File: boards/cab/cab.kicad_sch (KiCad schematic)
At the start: 44 parts, among them J1 Conn_01x08_Female, J2 Conn_01x08_Female, J3 Conn_01x08_Female, J4 Conn_01x08_Female, Q1 SI2308A, Q2 S8550, Q3 BC817-40,215, Q4 S8550, Q5 BC817-40,215, Q6 S8550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

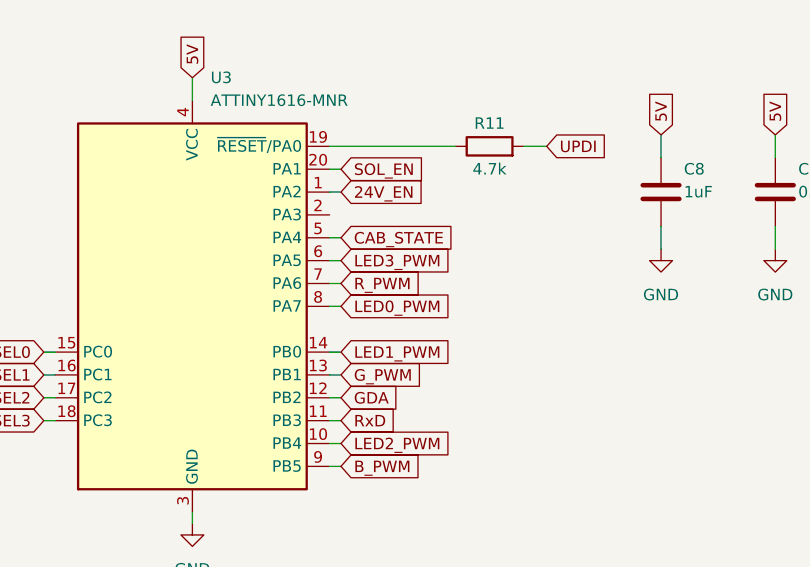
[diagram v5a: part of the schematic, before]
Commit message: Convert to 4 layer
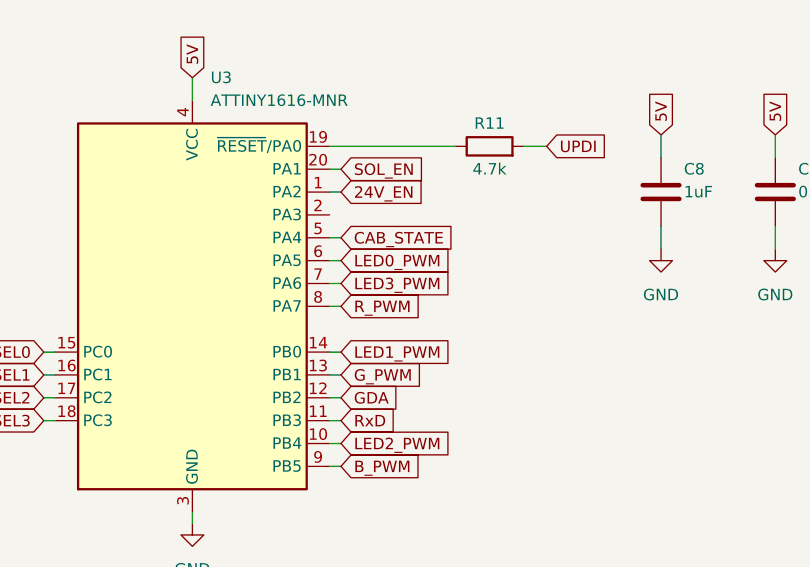
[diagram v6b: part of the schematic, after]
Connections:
- net LED0_PWM: now also U3.6 (PA5); no longer U3.8 (PA7)
- net LED3_PWM: now also U3.7 (PA6); no longer U3.6 (PA5)
- net R_PWM: now also U3.8 (PA7); no longer U3.7 (PA6)
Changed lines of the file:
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@@
+    )
+  )
+  (global_label "LED3_PWM" (shape input) (at 137.16 146.05 0) (fields_autoplaced)
+    (effects (font (size 1.27 1.27)) (justify left))
+    (property "Intersheet References" "${INTERSHEET_REFS}" (id 0) (at 149.3702 146.1294 0)
+      (effects (font (size 1.27 1.27)) (justify left) hide)
     )
   )
@@
     )
   )
+  (global_label "LED0_PWM" (shape input) (at 137.16 143.51 0) (fields_autoplaced)
+    (effects (font (size 1.27 1.27)) (justify left))
+    (property "Intersheet References" "${INTERSHEET_REFS}" (id 0) (at 149.3702 143.5894 0)
+      (effects (font (size 1.27 1.27)) (justify left) hide)
+    )
+  )
   (global_label "VBUS" (shape input) (at 26.67 76.2 180) (fields_autoplaced)
     (effects (font (size 1.27 1.27)) (justify right))
@@
     )
   )
-  (global_label "LED0_PWM" (shape input) (at 137.16 148.59 0) (fields_autoplaced)
-    (effects (font (size 1.27 1.27)) (justify left))
-    (property "Intersheet References" "${INTERSHEET_REFS}" (id 0) (at 149.3702 148.6694 0)
-      (effects (font (size 1.27 1.27)) (justify left) hide)
-    )
-  )
   (global_label "LED1_PWM" (shape input) (at 196.85 81.28 180) (fields_autoplaced)
     (effects (font (size 1.27 1.27)) (justify right))
@@
     )
   )
-  (global_label "R_PWM" (shape input) (at 137.16 146.05 0) (fields_autoplaced)
-    (effects (font (size 1.27 1.27)) (justify left))
-    (property "Intersheet References" "${INTERSHEET_REFS}" (id 0) (at 145.9836 146.1294 0)
-      (effects (font (size 1.27 1.27)) (justify left) hide)
-    )
-  )
   (global_label "G" (shape input) (at 204.47 30.48 0) (fields_autoplaced)
     (effects (font (size 1.27 1.27)) (justify left))
@@
     )
   )
+  (global_label "R_PWM" (shape input) (at 137.16 148.59 0) (fields_autoplaced)
+    (effects (font (size 1.27 1.27)) (justify left))
+    (property "Intersheet References" "${INTERSHEET_REFS}" (id 0) (at 145.9836 148.6694 0)
+      (effects (font (size 1.27 1.27)) (justify left) hide)
+    )
+  )
   (global_label "GDA" (shape input) (at 250.19 33.02 0) (fields_autoplaced)
     (effects (font (size 1.27 1.27)) (justify left))
@@
     )
   )
-  (global_label "LED3_PWM" (shape input) (at 137.16 143.51 0) (fields_autoplaced)
-    (effects (font (size 1.27 1.27)) (justify left))
-    (property "Intersheet References" "${INTERSHEET_REFS}" (id 0) (at 149.3702 143.5894 0)
-      (effects (font (size 1.27 1.27)) (justify left) hide)
-    )
-  )

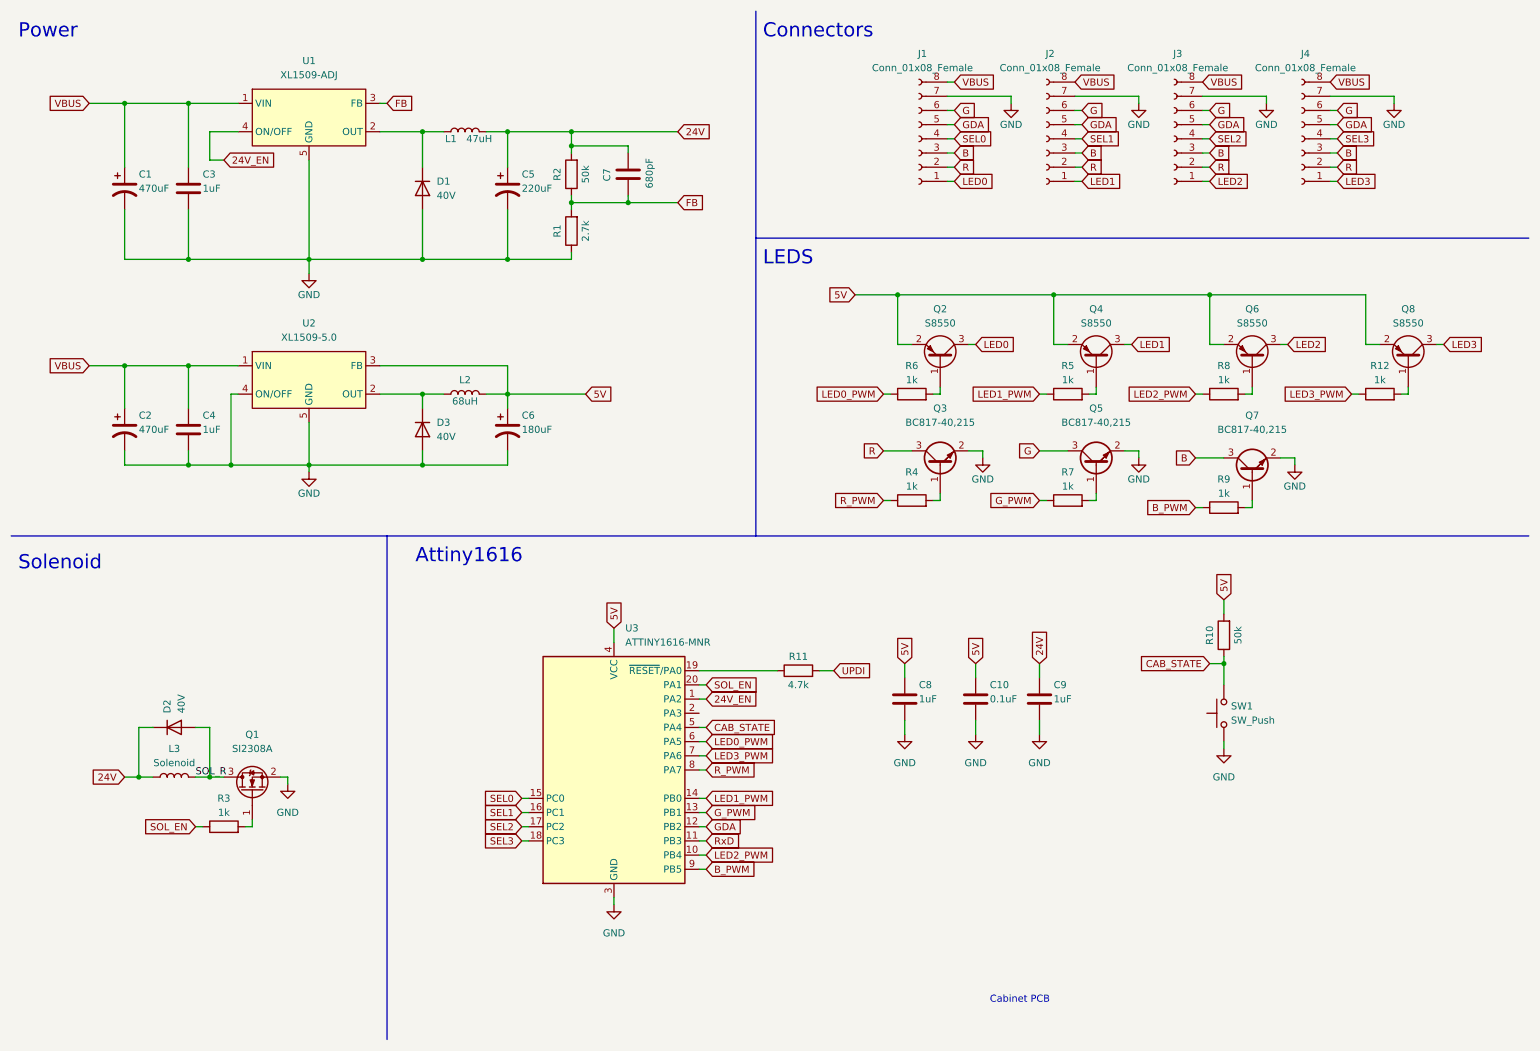
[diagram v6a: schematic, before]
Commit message: Added LED resistors, changed routing
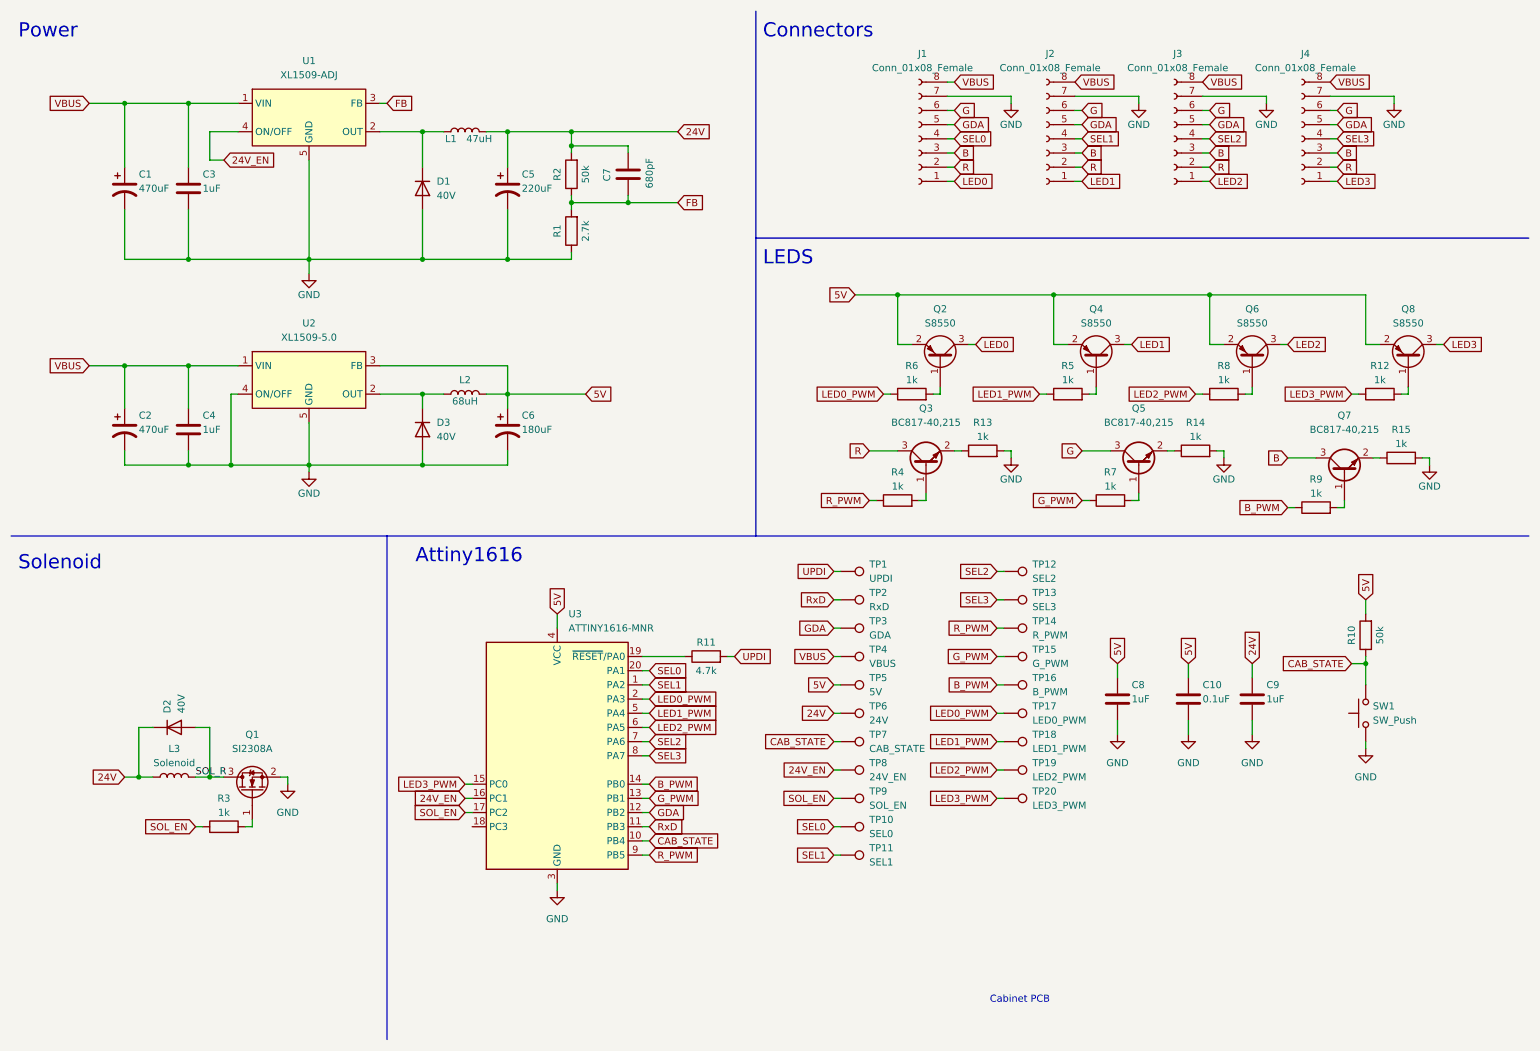
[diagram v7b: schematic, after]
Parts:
- added R13, R14, R15: 1k, Resistor_SMD:R_0805_2012Metric, symbol Device:R
- added TP1: UPDI, StackCabinet:testpad, symbol Connector:TestPoint
- added TP10: SEL0, StackCabinet:testpad, symbol Connector:TestPoint
- added TP11: SEL1, StackCabinet:testpad, symbol Connector:TestPoint
- added TP12: SEL2, StackCabinet:testpad, symbol Connector:TestPoint
- added TP13: SEL3, StackCabinet:testpad, symbol Connector:TestPoint
- added TP14: R_PWM, StackCabinet:testpad, symbol Connector:TestPoint
- added TP15: G_PWM, StackCabinet:testpad, symbol Connector:TestPoint
- added TP16: B_PWM, StackCabinet:testpad, symbol Connector:TestPoint
- added TP17: LED0_PWM, StackCabinet:testpad, symbol Connector:TestPoint
- added TP18: LED1_PWM, StackCabinet:testpad, symbol Connector:TestPoint
- added TP19: LED2_PWM, StackCabinet:testpad, symbol Connector:TestPoint
- added TP2: RxD, StackCabinet:testpad, symbol Connector:TestPoint
- added TP20: LED3_PWM, StackCabinet:testpad, symbol Connector:TestPoint
- added TP3: GDA, StackCabinet:testpad, symbol Connector:TestPoint
- added TP4: VBUS, StackCabinet:testpad, symbol Connector:TestPoint
- added TP5: 5V, StackCabinet:testpad, symbol Connector:TestPoint
- added TP6: 24V, StackCabinet:testpad, symbol Connector:TestPoint
- added TP7: CAB_STATE, StackCabinet:testpad, symbol Connector:TestPoint
- added TP8: 24V_EN, StackCabinet:testpad, symbol Connector:TestPoint
- added TP9: SOL_EN, StackCabinet:testpad, symbol Connector:TestPoint
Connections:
- net 24V: now also TP6.1
- net 24V_EN: now also U3.16 (PC1), TP8.1; no longer U3.1 (PA2)
- net 5V: now also TP5.1
- net B_PWM: now also U3.14 (PB0), TP16.1; no longer U3.9 (PB5)
- net CAB_STATE: now also U3.10 (PB4), TP7.1; no longer U3.5 (PA4)
- net GDA: now also TP3.1
- net GND: now also R13.2, R14.2, R15.2; no longer Q3.2 (E), Q5.2 (E), Q7.2 (E)
- net G_PWM: now also TP15.1
- net LED0_PWM: now also U3.2 (PA3), TP17.1; no longer U3.6 (PA5)
- net LED1_PWM: now also U3.5 (PA4), TP18.1; no longer U3.14 (PB0)
- net LED2_PWM: now also U3.6 (PA5), TP19.1; no longer U3.10 (PB4)
- net LED3_PWM: now also U3.15 (PC0), TP20.1; no longer U3.7 (PA6)
- net R_PWM: now also U3.9 (PB5), TP14.1; no longer U3.8 (PA7)
- net RxD: now also TP2.1
- net SEL0: now also U3.20 (PA1), TP10.1; no longer U3.15 (PC0)
- net SEL1: now also U3.1 (PA2), TP11.1; no longer U3.16 (PC1)
- net SEL2: now also U3.7 (PA6), TP12.1; no longer U3.17 (PC2)
- net SEL3: now also U3.8 (PA7), TP13.1; no longer U3.18 (PC3)
- net SOL_EN: now also U3.17 (PC2), TP9.1; no longer U3.20 (PA1)
- net UPDI: now also TP1.1
- net VBUS: now also TP4.1
- new net: Q3.2 (E), R13.1
- new net: Q5.2 (E), R14.1
- new net: Q7.2 (E), R15.1
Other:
- moved on the sheet: C10, C8, C9, Q3, Q5, Q7, R10, R11, R4, R7, R9, SW1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

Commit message: Added silklayer text and generated gerber
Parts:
- U1, U2: footprint Package_SO:SOP-8_3.9x4.9mm_P1.27mm -> StackCabinet:XLE1509
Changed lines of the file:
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@@
     (property "Reference" "U2" (id 0) (at 66.04 68.58 0))
     (property "Value" "XL1509-5.0" (id 1) (at 66.04 71.12 0))
-    (property "Footprint" "Package_SO:SOP-8_3.9x4.9mm_P1.27mm" (id 2) (at 66.04 60.96 0)
+    (property "Footprint" "StackCabinet:XLE1509" (id 2) (at 66.04 60.96 0)
       (effects (font (size 1.27 1.27)) hide)
     )
@@
     (property "Reference" "U1" (id 0) (at 66.04 21.59 0))
     (property "Value" "XL1509-ADJ" (id 1) (at 66.04 24.13 0))
-    (property "Footprint" "Package_SO:SOP-8_3.9x4.9mm_P1.27mm" (id 2) (at 66.04 13.97 0)
+    (property "Footprint" "StackCabinet:XLE1509" (id 2) (at 66.04 13.97 0)
       (effects (font (size 1.27 1.27)) hide)
     )
@@
     )
     (path "/d9251f9c-6022-402f-b111-d7ea029f5bed"
-      (reference "U1") (unit 1) (value "XL1509-ADJ") (footprint "Package_SO:SOP-8_3.9x4.9mm_P1.27mm")
+      (reference "U1") (unit 1) (value "XL1509-ADJ") (footprint "StackCabinet:XLE1509")
     )
     (path "/8acf6c01-51de-4e79-b903-1dfc399c51f5"
-      (reference "U2") (unit 1) (value "XL1509-5.0") (footprint "Package_SO:SOP-8_3.9x4.9mm_P1.27mm")
+      (reference "U2") (unit 1) (value "XL1509-5.0") (footprint "StackCabinet:XLE1509")
     )
     (path "/a9781253-aec5-40b2-9c6f-6516d5c04024"
